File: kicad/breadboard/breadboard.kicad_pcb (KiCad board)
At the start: 2 copper layers, 100 x 100 mm, 22 parts, among them J1 Conn_01x08, J3 Conn_01x08, J4 Conn_01x30, J49 Barrel_Jack, J5 Conn_01x30, J6 Conn_01x30, J7 Conn_01x30, SW1 SWITCH, SW2 SWITCH, U1 AMS1117-3V3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

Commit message: breadboard: add net class power
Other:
- net class Power added: clearance 0.25, trace_width 0.381, via_dia 0.4, via_drill 0.3
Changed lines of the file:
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@@
-(kicad_pcb (version 4) (host pcbnew 4.0.7)
+(kicad_pcb (version 4) (host pcbnew 4.0.7-e2-6376~58~ubuntu16.04.1)
   (general
     (links 407)
     (no_connects 0)
-    (area 84.924999 32.424999 185.075001 132.575001)
+    (area 84.924999 30.81238 185.075001 133.017619)
     (thickness 1.6)
     (drawings 7)
@@
     (add_net VCC)
   )
+  (net_class Power ""
+    (clearance 0.25)
+    (trace_width 0.381)
+    (via_dia 0.4)
+    (via_drill 0.3)
+    (uvia_dia 0.3)
+    (uvia_drill 0.1)
+  )
   (module breadboard:bboard_3rows_footprint (layer F.Cu)

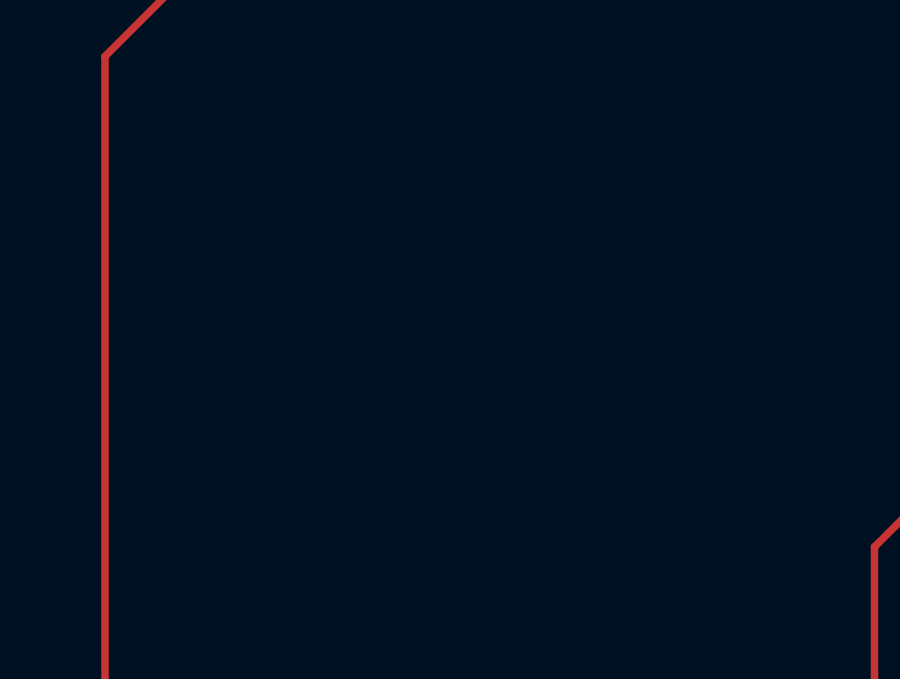
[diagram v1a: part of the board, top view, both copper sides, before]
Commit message: breadboard: fix the mistakes in esp12e board design
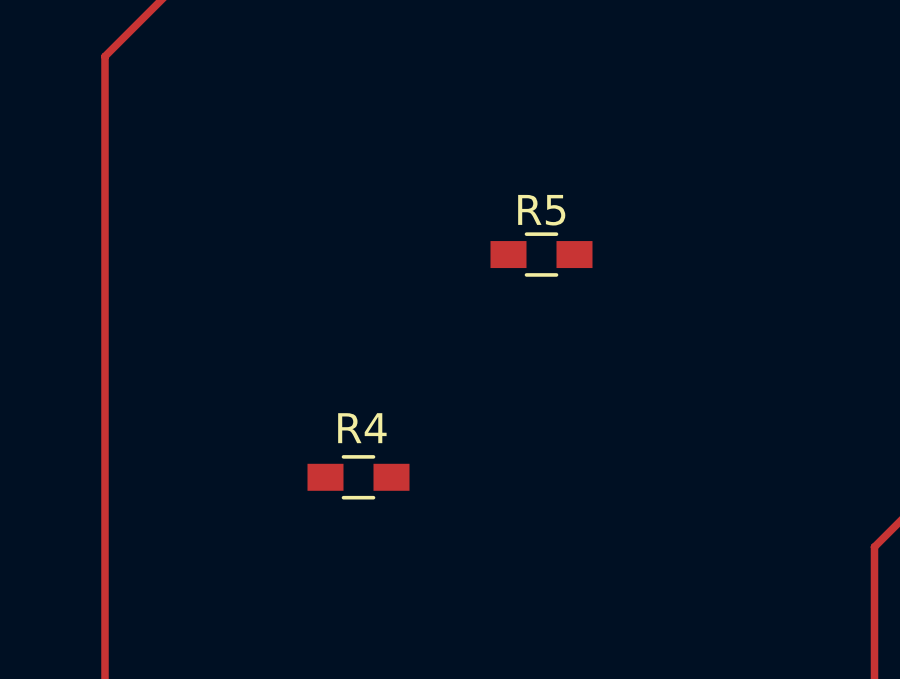
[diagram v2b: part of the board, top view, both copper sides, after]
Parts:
- added R4: R, Resistors_SMD:R_0603_HandSoldering, F.Cu at (103.7, 78.8)
- added R5: R, Resistors_SMD:R_0603_HandSoldering, F.Cu at (109.8, 71.4)
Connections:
- net Net-(J1-Pad1) renamed /esp12e/RST
- net Net-(J1-Pad2) renamed /esp12e/ADC
- net Net-(J1-Pad3) renamed /esp12e/CH_PD
- net Net-(J1-Pad4) renamed /esp12e/GPIO16
- net Net-(J1-Pad5) renamed /esp12e/GPIO14
- net Net-(J1-Pad6) renamed /esp12e/GPIO12
- net Net-(J1-Pad7) renamed /esp12e/GPIO13
- net Net-(J3-Pad2) renamed /esp12e/GPIO15
- net Net-(J3-Pad3) renamed /esp12e/GPIO2
- net Net-(J3-Pad4) renamed /esp12e/GPIO0
- net Net-(J3-Pad5) renamed /esp12e/GPIO4
- net Net-(J3-Pad6) renamed /esp12e/GPIO5
- net Net-(J3-Pad7) renamed /esp12e/RXD
- net Net-(J3-Pad8) renamed /esp12e/TXD
